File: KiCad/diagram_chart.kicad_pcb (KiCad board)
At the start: 2 copper layers, 120 x 120 mm, 115 parts, among them SW0 SW0, SW1 SW1, SW2 SW2, SW3 SW3, SW4 SW4, SW5 SW5, SW6 SW6, SW7 SW7, U1 TPIC6C595, U2 74HC165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

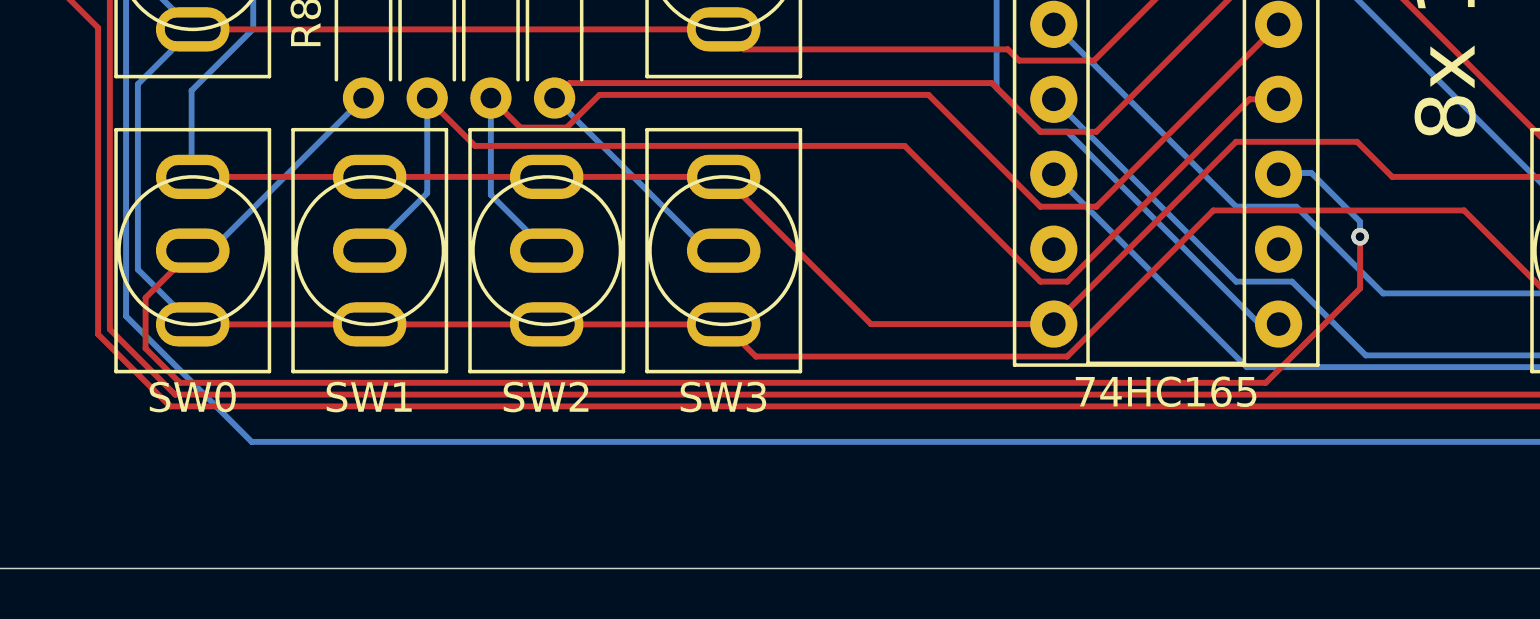
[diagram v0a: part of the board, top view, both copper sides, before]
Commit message: Ordered via JLCPCB Used GERBERS inside ZIP. Realized it is chinese new years.
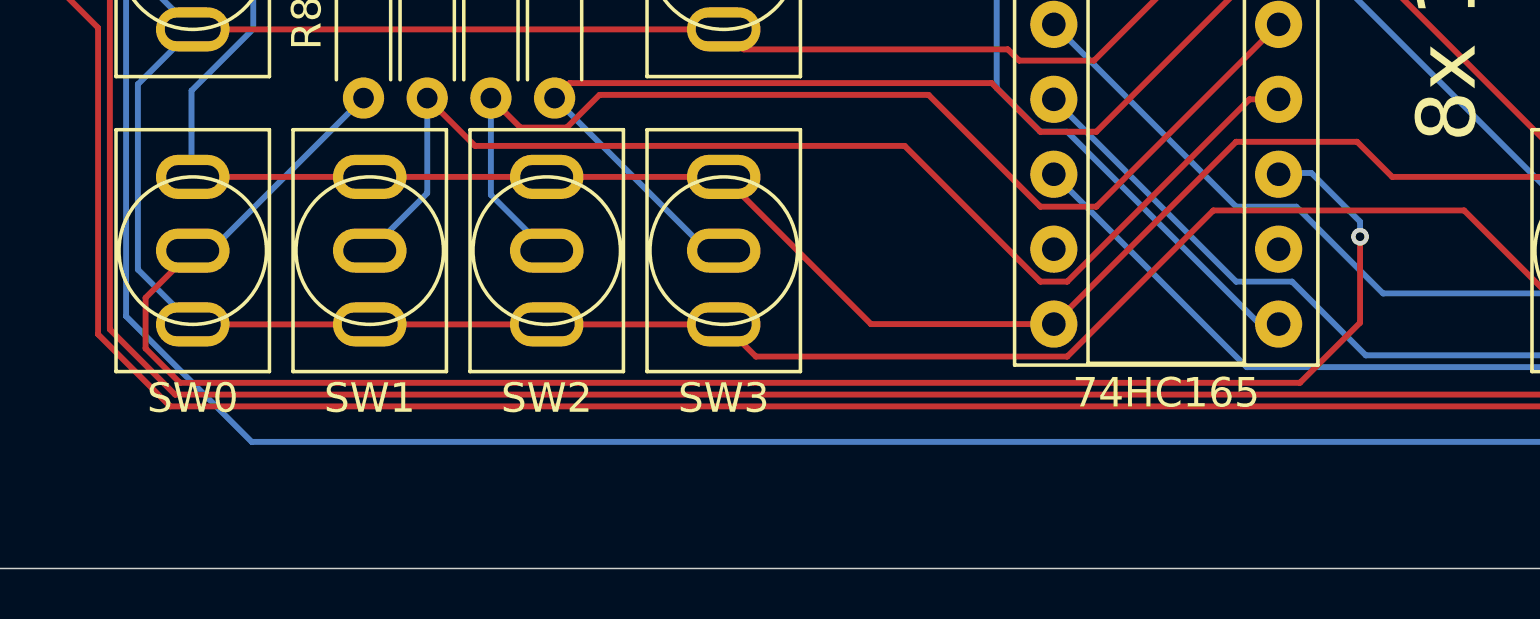
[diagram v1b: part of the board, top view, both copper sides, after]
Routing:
- net Net-(SW0-B): track 61.1 -> 61.8 mm
